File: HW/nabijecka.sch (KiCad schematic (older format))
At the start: 12 parts

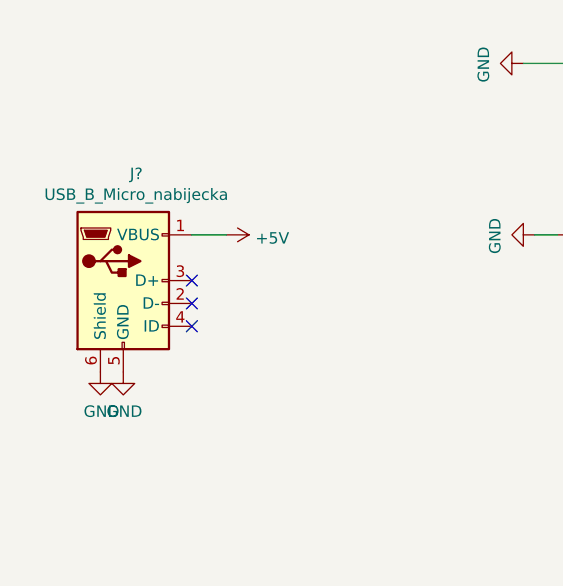
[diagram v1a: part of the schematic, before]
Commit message: change USB
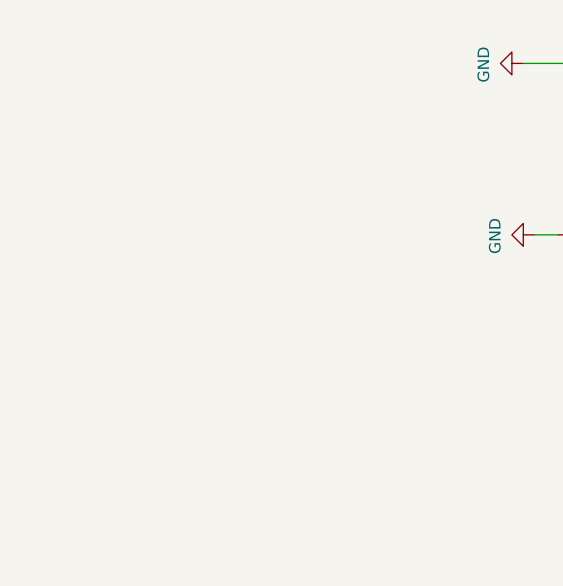
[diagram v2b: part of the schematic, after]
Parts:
- removed J?: USB_B_Micro_nabijecka, symbol Connector:USB_B_Micro
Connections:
- no-connect marks 3 -> 0
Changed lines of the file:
@@
 $Descr A4 11693 8268
 encoding utf-8
-Sheet 9 16
+Sheet 16 17
 Title ""
 Date ""
@@
 Comment4 ""
 $EndDescr
-$Comp
-L Connector:USB_B_Micro J?
-U 1 1 5F752228
-P 1400 3400
-F 0 "J?" H 1457 3867 50  0000 C CNN
-F 1 "USB_B_Micro_nabijecka" H 1457 3776 50  0000 C CNN
-F 2 "" H 1550 3350 50  0001 C CNN
-F 3 "~" H 1550 3350 50  0001 C CNN
-	1    1400 3400
-	1    0    0    -1
-$EndComp
-$Comp
-L power:GND #PWR?
-U 1 1 5F75334B
-P 1400 3800
-F 0 "#PWR?" H 1400 3550 50  0001 C CNN
-F 1 "GND" H 1405 3627 50  0000 C CNN
-F 2 "" H 1400 3800 50  0001 C CNN
-F 3 "" H 1400 3800 50  0001 C CNN
-	1    1400 3800
-	1    0    0    -1
-$EndComp
-$Comp
-L power:GND #PWR?
-U 1 1 5F7535E3
-P 1300 3800
-F 0 "#PWR?" H 1300 3550 50  0001 C CNN
-F 1 "GND" H 1305 3627 50  0000 C CNN
-F 2 "" H 1300 3800 50  0001 C CNN
-F 3 "" H 1300 3800 50  0001 C CNN
-	1    1300 3800
-	1    0    0    -1
-$EndComp
-$Comp
-L power:+5V #PWR?
-U 1 1 5F753B82
-P 1850 3200
-F 0 "#PWR?" H 1850 3050 50  0001 C CNN
-F 1 "+5V" V 1865 3328 50  0000 L CNN
-F 2 "" H 1850 3200 50  0001 C CNN
-F 3 "" H 1850 3200 50  0001 C CNN
-	1    1850 3200
-	0    1    1    0
-$EndComp
 $Comp
 L power:+5V #PWR?
@@
 	1    0    0    -1
 $EndComp
-Wire Wire Line
-	1850 3200 1700 3200
-NoConn ~ 1700 3400
-NoConn ~ 1700 3500
-NoConn ~ 1700 3600
 $Comp
 L symbols:TP4056 U?

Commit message: add some packages
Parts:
- C? (x2): footprint (none) -> Capacitor_SMD:C_1206_3216Metric
- D? (x2): footprint (none) -> LED_SMD:LED_0603_1608Metric
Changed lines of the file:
@@
 $Descr A4 11693 8268
 encoding utf-8
-Sheet 16 42
+Sheet 14 42
 Title ""
 Date ""
@@
 F 0 "D?" H 5293 2045 50  0000 C CNN
 F 1 "green" H 5293 2136 50  0000 C CNN
-F 2 "" H 5300 2300 50  0001 C CNN
+F 2 "LED_SMD:LED_0603_1608Metric" H 5300 2300 50  0001 C CNN
 F 3 "~" H 5300 2300 50  0001 C CNN
 	1    5300 2300
@@
 F 0 "C?" H 5365 3796 50  0000 L CNN
 F 1 "10u" H 5365 3705 50  0000 L CNN
-F 2 "" H 5288 3600 50  0001 C CNN
+F 2 "Capacitor_SMD:C_1206_3216Metric" H 5288 3600 50  0001 C CNN
 F 3 "~" H 5250 3750 50  0001 C CNN
 	1    5250 3750
@@
 F 0 "C?" V 3298 2450 50  0000 C CNN
 F 1 "10u" V 3389 2450 50  0000 C CNN
-F 2 "" H 3588 2300 50  0001 C CNN
+F 2 "Capacitor_SMD:C_1206_3216Metric" H 3588 2300 50  0001 C CNN
 F 3 "~" H 3550 2450 50  0001 C CNN
 	1    3550 2450
@@
 F 0 "D?" H 5293 2395 50  0000 C CNN
 F 1 "red" H 5293 2486 50  0000 C CNN
-F 2 "" H 5300 2650 50  0001 C CNN
+F 2 "LED_SMD:LED_0603_1608Metric" H 5300 2650 50  0001 C CNN
 F 3 "~" H 5300 2650 50  0001 C CNN
 	1    5300 2650

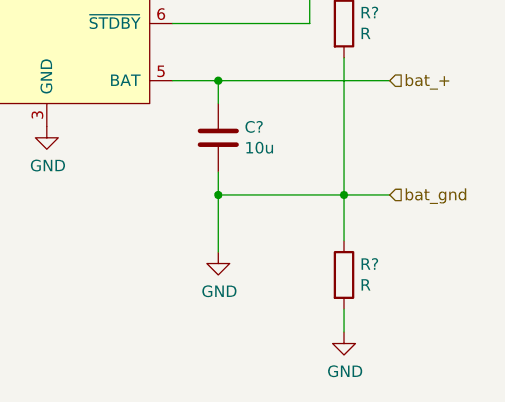
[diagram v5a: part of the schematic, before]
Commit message: add polyfuse for battery, remove resistor by SY8105, fix mistake by charger
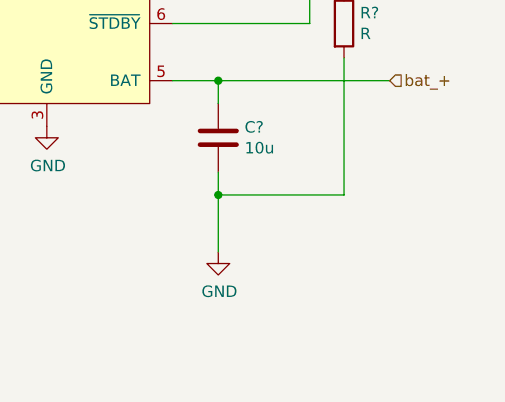
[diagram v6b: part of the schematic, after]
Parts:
- removed R?: R, Resistor_SMD:R_0402_1005Metric, symbol Device:R
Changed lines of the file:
@@
-$Comp
-L Device:R R?
-U 1 1 5F729FE7
-P 5800 4350
-F 0 "R?" H 5870 4396 50  0000 L CNN
-F 1 "R" H 5870 4305 50  0000 L CNN
-F 2 "Resistor_SMD:R_0402_1005Metric" V 5730 4350 50  0001 C CNN
-F 3 "~" H 5800 4350 50  0001 C CNN
-	1    5800 4350
-	1    0    0    -1
-$EndComp
-$Comp
-L power:GND #PWR?
-U 1 1 5F72ACF6
-P 5800 4600
-F 0 "#PWR?" H 5800 4350 50  0001 C CNN
-F 1 "GND" H 5805 4427 50  0000 C CNN
-F 2 "" H 5800 4600 50  0001 C CNN
-F 3 "" H 5800 4600 50  0001 C CNN
-	1    5800 4600
-	1    0    0    -1
-$EndComp
-Wire Wire Line
-	5800 4600 5800 4500
 $Comp
 L Device:R R?
@@
 Wire Wire Line
 	3400 2450 3150 2450
-Text HLabel 6000 4000 2    50   Input ~ 0
-bat_gnd
 Wire Wire Line
 	5800 3400 5800 4000
@@
 	5250 3900 5250 4000
 Wire Wire Line
-	6000 4000 5800 4000
-Connection ~ 5800 4000
-Wire Wire Line
-	5800 4200 5800 4000
-Wire Wire Line
 	5800 4000 5250 4000
